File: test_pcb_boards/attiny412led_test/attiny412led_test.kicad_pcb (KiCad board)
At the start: 2 copper layers, 7 parts, among them J1 Conn_PinHeader_1x02_P2.54mm_H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, J2 Conn_PinHeader_1x02_P2.54mm_H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, J3 Conn_PinHeader_1x05_P2.54mm_H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, U1 Microcontroller_ATtiny412_SSFR

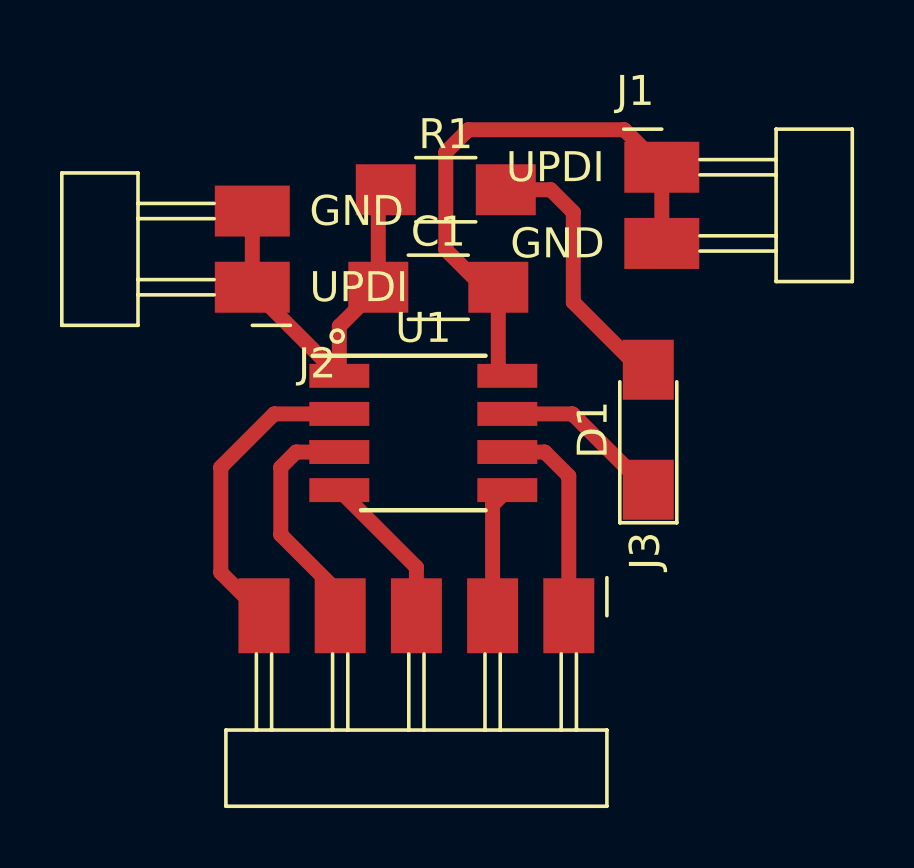
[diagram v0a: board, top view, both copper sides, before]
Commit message: added edge cuts to 412 led test
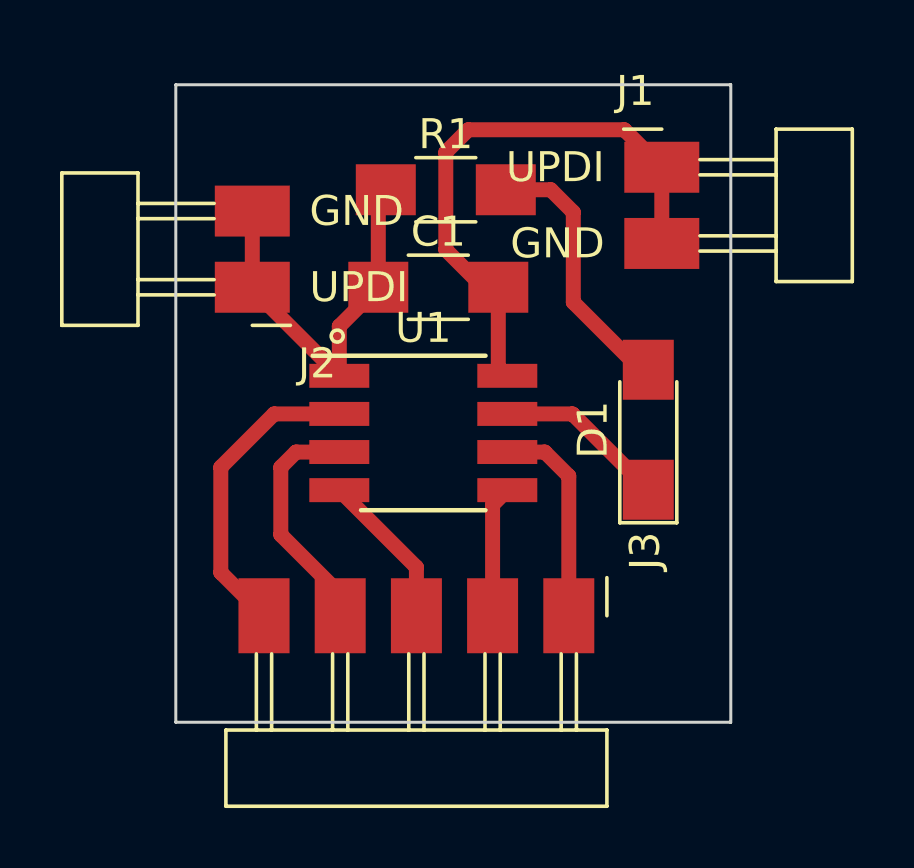
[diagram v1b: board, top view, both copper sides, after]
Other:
- board outline added: 18.5 x 21.2 mm
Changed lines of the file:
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@@
     (pad_to_mask_clearance 0)
     (pcbplotparams
-      (layerselection 0x00010fc_ffffffff)
+      (layerselection 0x0001000_7fffffff)
       (disableapertmacros false)
       (usegerberextensions false)
@@
       (outputformat 1)
       (mirror false)
-      (drillshape 1)
+      (drillshape 0)
       (scaleselection 1)
       (outputdirectory "")
@@
     )
   )
+  (gr_rect (start 125.5 92.75) (end 107 71.5) (layer "Edge.Cuts") (width 0.1) (fill none))
   (segment (start 118 75) (end 119.5 75) (width 0.5) (layer "F.Cu") (net 1))
   (segment (start 120.25 75.75) (end 120.25 78.75) (width 0.5) (layer "F.Cu") (net 1))
